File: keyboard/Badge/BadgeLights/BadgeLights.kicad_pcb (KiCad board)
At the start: 2 copper layers, 134 x 12 mm, 24 parts, among them U1 ATtiny85-20P

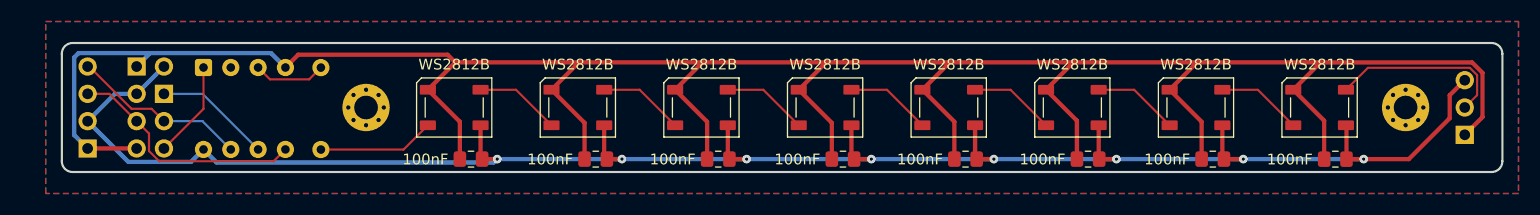
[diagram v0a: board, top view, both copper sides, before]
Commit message: Update badgelight board for I2C out
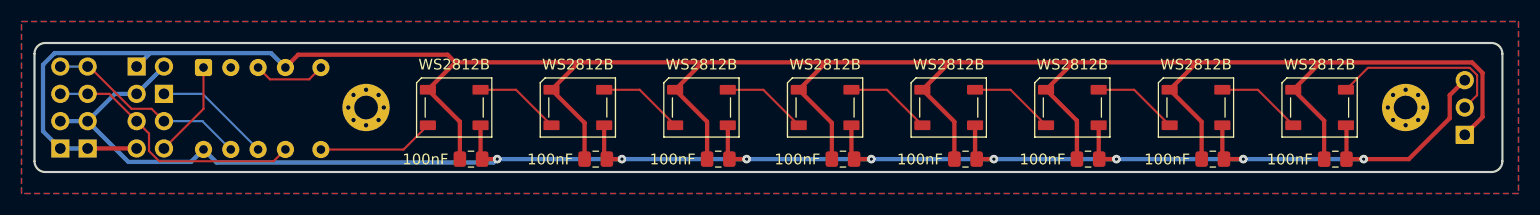
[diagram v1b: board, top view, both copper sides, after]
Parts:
- added qwiic: Conn_01x04, Connector_PinHeader_2.54mm:PinHeader_1x04_P2.54mm_Vertical, B.Cu at (37.9, 71.3)
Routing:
- net GND: track 245.0 -> 250.2 mm
- net +5V: track 182.6 -> 185.1 mm
- net Net-(J1-Pin_4): track 22.4 -> 24.9 mm
- net Net-(J1-Pin_3): track 16.5 -> 19.1 mm
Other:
- board size 134 x 12 mm -> 136.5 x 12 mm
